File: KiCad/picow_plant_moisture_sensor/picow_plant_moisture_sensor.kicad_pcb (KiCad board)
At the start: 4 copper layers, 94.6 x 64.1 mm, 64 parts, among them J1 Conn_01x03, J10 Conn_01x03, J11 Conn_01x03, J12 Conn_01x03, J13 Conn_02x03_Odd_Even, J14 Conn_01x03, J15 Conn_01x03, J16 Conn_01x03, J17 Conn_01x03, J2 Conn_01x03, J3 Conn_01x03, J4 Conn_01x03, J5 Conn_01x03, J6 Conn_01x03, J7 Conn_01x03, J8 Conn_01x03, J9 Conn_01x03, SW1 SW_Push, SW2 SW_Push, SW3 SW_Push, SW4 SW_Push, U1 ADS1115IDGS, U2 PicoW, U3 ADS1115IDGS, U4 ADS1115IDGS, U5 ADS1115IDGS, U6 24LC16

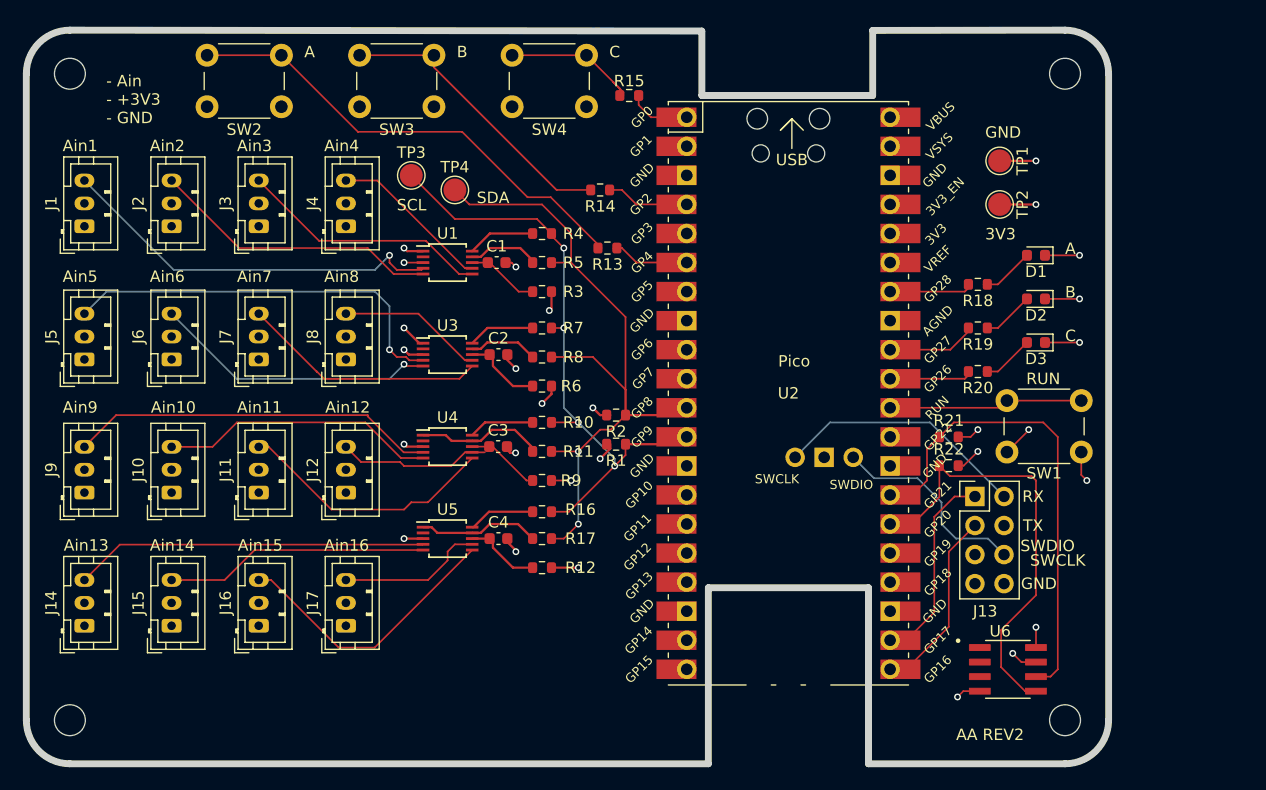
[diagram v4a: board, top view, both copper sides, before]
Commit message: 32 board bring up (#35)
* Add rev2

* Add eeprom cap and I2C test points
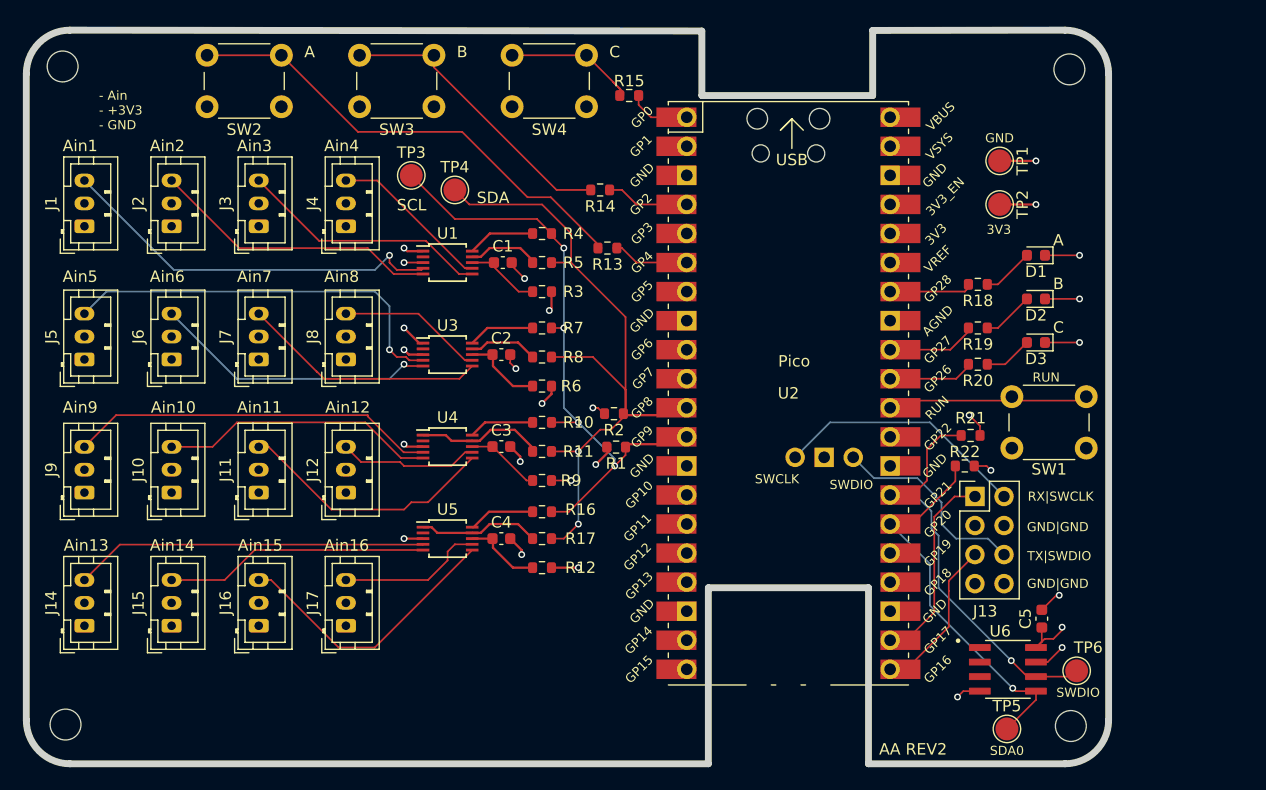
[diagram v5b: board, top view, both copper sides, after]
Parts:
- added C5: 100n, Capacitor_SMD:C_0603_1608Metric, F.Cu at (152.6, 94.7)
- added TP5: TestPoint, TestPoint:TestPoint_Pad_D2.0mm, F.Cu at (149.6, 104.3)
- added TP6: TestPoint, TestPoint:TestPoint_Pad_D2.0mm, F.Cu at (155.7, 99.3)
- moved R21 1.91 mm to (146.4, 78.7)
- moved R22 1.40 mm to (145.9, 81.4)
- moved H2 0.90 mm to (67.0, 46.4)
- moved H3 0.72 mm to (155.2, 104.1)
- moved R20 0.63 mm to (147.1, 72.5)
- moved SW1 0.55 mm to (150.0, 75.3)
- moved H1 0.54 mm to (155.1, 46.7)
- moved H4 0.54 mm to (67.3, 104.0)
- moved C1 0.54 mm to (105.5, 63.6)
- moved C3 0.28 mm to (105.4, 79.7)
- moved C2 0.25 mm to (105.4, 71.6)
- moved C4 0.25 mm to (105.4, 87.7)
- moved R1 0.25 mm to (115.4, 79.7)
- moved R2 0.23 mm to (115.2, 76.8)
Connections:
- J13 pad 3: /GPIO16 -> GND
- J13 pad 5: GND -> /GPIO16
- TP3 pad 1: /SCL -> /GPIO9
- TP4 pad 1: /SDA -> /GPIO8
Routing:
- net /GPIO21: track 41.9 -> 36.6 mm, vias 0 -> 1
- net /GPIO20: track 38.5 -> 33.9 mm, vias 0 -> 1
- net +3V3: track 22.4 -> 25.6 mm
- net GND: track 37.7 -> 34.8 mm, vias 17 -> 16
- net /GPIO16: track 16.5 -> 13.9 mm
- net /AIN8: track 33.3 -> 32.2 mm
- net Net-(D3-A): track 4.83 -> 4.26 mm
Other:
- board text added: "GND|GND"
- board text added: "RX|SWCLK"
- board text added: "SDA0"
- board text added: "TX|SWDIO"
- board text removed: "RX"
- board text removed: "SWCLK"
- board text removed: "TX"

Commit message: Design with RP2040 IC instead of pico board
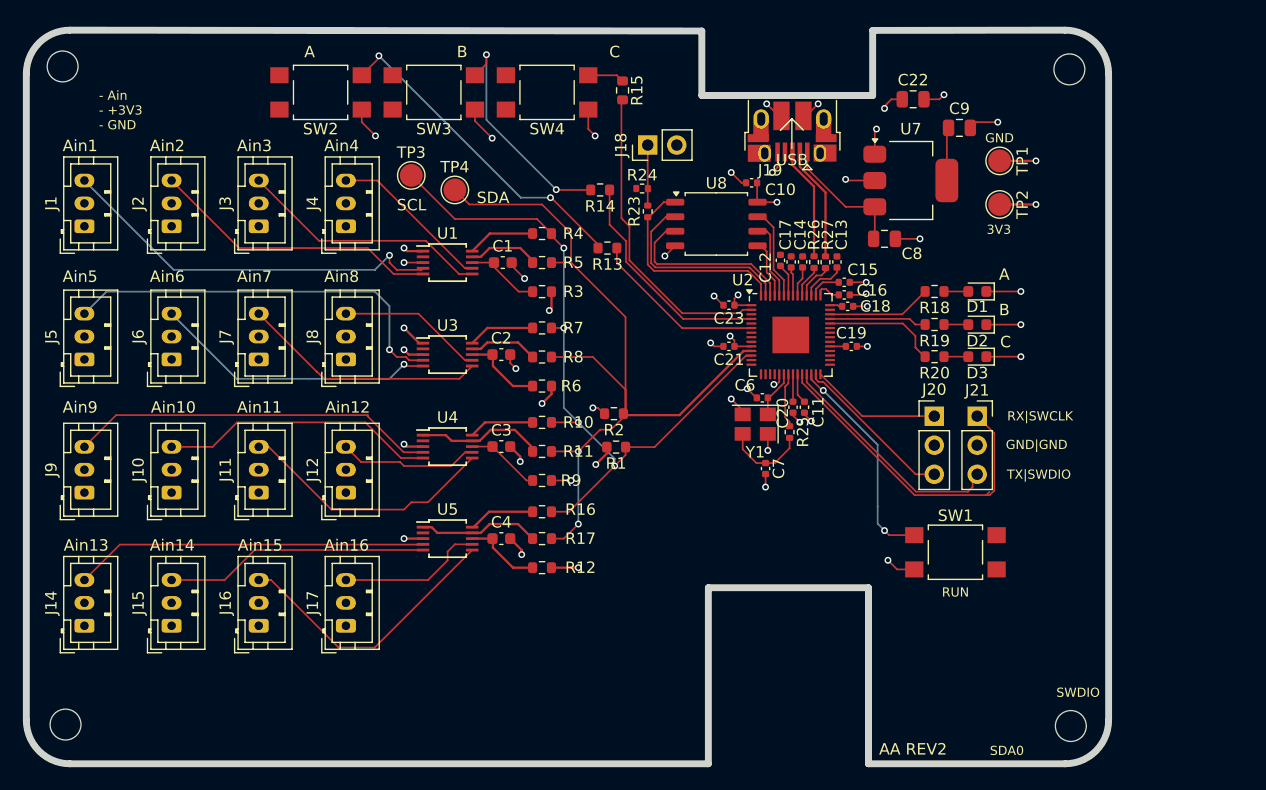
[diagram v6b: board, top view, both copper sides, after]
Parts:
- removed C5: 100n, Capacitor_SMD:C_0603_1608Metric
- removed J13: Conn_02x03_Odd_Even, Connector_PinHeader_2.54mm:PinHeader_2x04_P2.54mm_Vertical
- removed R21, R22: 5k, Resistor_SMD:R_0603_1608Metric
- removed TP5, TP6: TestPoint, TestPoint:TestPoint_Pad_D2.0mm
- removed U6: 24LC16, 24LC16B-I_SN:SOIC127P600X175-8N
- added C10: 100n, Capacitor_SMD:C_0402_1005Metric, F.Cu at (127.3, 56.6)
- added C11: 100n, Capacitor_SMD:C_0402_1005Metric, F.Cu at (131.9, 76.2)
- added C12: 100n, Capacitor_SMD:C_0402_1005Metric, F.Cu at (129.8, 63.4)
- added C13: 1u, Capacitor_SMD:C_0402_1005Metric, F.Cu at (134.7, 63.5)
- added C14: 100n, Capacitor_SMD:C_0402_1005Metric, F.Cu at (131.7, 63.5)
- added C15: 1u, Capacitor_SMD:C_0402_1005Metric, F.Cu at (135.4, 65.3)
- added C16: 100n, Capacitor_SMD:C_0402_1005Metric, F.Cu at (135.4, 66.4)
- added C17: 100n, Capacitor_SMD:C_0402_1005Metric, F.Cu at (130.7, 63.5)
- added C18: 100n, Capacitor_SMD:C_0402_1005Metric, F.Cu at (135.7, 67.4)
- added C19: 100n, Capacitor_SMD:C_0402_1005Metric, F.Cu at (136.0, 70.9)
- added C20: 100n, Capacitor_SMD:C_0402_1005Metric, F.Cu at (130.9, 76.2)
- added C21: 100n, Capacitor_SMD:C_0402_1005Metric, F.Cu at (125.3, 70.9)
- added C22: 10u, Capacitor_SMD:C_0805_2012Metric, F.Cu at (141.4, 49.3)
- added C23: 100n, Capacitor_SMD:C_0402_1005Metric, F.Cu at (125.3, 67.3)
- added C6: 15p, Capacitor_SMD:C_0402_1005Metric, F.Cu at (128.2, 75.4)
- added C7: 15p, Capacitor_SMD:C_0402_1005Metric, F.Cu at (128.5, 81.6)
- added C8: 10u, Capacitor_SMD:C_0805_2012Metric, F.Cu at (138.9, 61.5)
- added C9: 10u, Capacitor_SMD:C_0805_2012Metric, F.Cu at (145.4, 51.8)
- added J18: Conn_01x02, Connector_PinHeader_2.54mm:PinHeader_1x02_P2.54mm_Vertical, F.Cu at (118.2, 53.3)
- added J19: USB_B_Micro, Connector_USB:USB_Micro-B_Amphenol_10103594-0001LF_Horizontal, F.Cu at (130.8, 52.1)
- added J20: Conn_01x03, Connector_PinHeader_2.54mm:PinHeader_1x03_P2.54mm_Vertical, F.Cu at (143.2, 77.0)
- added J21: Conn_01x03, Connector_PinSocket_2.54mm:PinSocket_1x03_P2.54mm_Vertical, F.Cu at (147.0, 77.0)
- added R23: 1k, Resistor_SMD:R_0402_1005Metric, F.Cu at (118.2, 59.1)
- added R24: DNF, Resistor_SMD:R_0402_1005Metric, F.Cu at (117.7, 57.1)
- added R25: 1k, Resistor_SMD:R_0402_1005Metric, F.Cu at (130.6, 78.4)
- added R26: 27, Resistor_SMD:R_0402_1005Metric, F.Cu at (132.7, 63.5)
- added R27: 27, Resistor_SMD:R_0402_1005Metric, F.Cu at (133.7, 63.5)
- added U7: NCP1117-3.3_SOT223, Package_TO_SOT_SMD:SOT-223-3_TabPin2, F.Cu at (141.2, 56.4)
- added U8: W25Q128JVS, Package_SO:SOIC-8_5.23x5.23mm_P1.27mm, F.Cu at (124.2, 60.2)
- added Y1: ABM8-272-T3, Crystal:Crystal_SMD_3225-4Pin_3.2x2.5mm, F.Cu at (127.6, 77.7)
- SW1, SW2, SW3, SW4: footprint Button_Switch_THT:SW_PUSH_6mm -> Button_Switch_SMD:SW_SPST_TL3305A
- U2: value PicoW -> RP2040; footprint RaspberryPI PicoW:RPi_PicoW_SMD_TH -> Package_DFN_QFN:QFN-56-1EP_7x7mm_P0.4mm_EP3.2x3.2mm
- moved SW1 14.5 mm to (145.1, 88.9)
- moved D1 6.02 mm to (147.0, 66.1)
- moved D2 5.60 mm to (147.0, 69.0)
- moved D3 5.28 mm to (147.0, 71.8)
- moved U2 5.10 mm to (130.7, 69.9)
- moved R20 3.84 mm to (143.3, 71.8)
- moved R18 3.84 mm to (143.3, 66.1)
- moved R19 3.80 mm to (143.3, 69.0)
- moved SW4 3.66 mm to (109.4, 48.7)
- moved SW2 3.65 mm to (89.6, 48.7)
- moved SW3 1.25 mm to (99.5, 48.7)
- moved R15 0.73 mm to (116.0, 48.5), turned to 90 degrees
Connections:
- net /GPIO8 renamed /SDA1
- net /GPIO9 renamed /SCL1
- R18 pad 2: /GPIO28 -> /MCU/GPIO28
- R19 pad 2: /GPIO27 -> /MCU/GPIO27
- R20 pad 2: /GPIO26 -> /MCU/GPIO26
- SW1 pad 1: /RUN -> Net-(U2-RUN)
- U2 pad 1: /GPIO0 -> +3V3
- U2 pad 10: /GPIO7 -> +3V3
- U2 pad 13: GND -> unconnected-(U2-GPIO10-Pad13)
- U2 pad 14: /GPIO10 -> unconnected-(U2-GPIO11-Pad14)
- U2 pad 15: /GPIO11 -> unconnected-(U2-GPIO12-Pad15)
- U2 pad 16: /GPIO12 -> unconnected-(U2-GPIO13-Pad16)
- U2 pad 17: /GPIO13 -> unconnected-(U2-GPIO14-Pad17)
- U2 pad 18: GND -> unconnected-(U2-GPIO15-Pad18)
- U2 pad 19: /GPIO14 -> GND
- U2 pad 2: /GPIO1 -> /GPIO0
- U2 pad 20: /GPIO15 -> /MCU/XIN
- U2 pad 21: /GPIO16 -> /MCU/XOUT
- U2 pad 22: /GPIO17 -> +3V3
- U2 pad 23: GND -> +1V1
- U2 pad 24: /GPIO18 -> /MCU/SWCLK
- U2 pad 25: /GPIO19 -> /MCU/SWD
- U2 pad 26: /GPIO20 -> Net-(U2-RUN)
- U2 pad 27: /GPIO21 -> /MCU/UART0_TX
- U2 pad 28: GND -> /MCU/UART0_RX
- U2 pad 29: /GPIO22 -> unconnected-(U2-GPIO18-Pad29)
- U2 pad 3: GND -> unconnected-(U2-GPIO1-Pad3)
- U2 pad 30: /RUN -> unconnected-(U2-GPIO19-Pad30)
- U2 pad 31: /GPIO26 -> unconnected-(U2-GPIO20-Pad31)
- U2 pad 32: /GPIO27 -> unconnected-(U2-GPIO21-Pad32)
- U2 pad 33: GND -> +3V3
- U2 pad 34: /GPIO28 -> unconnected-(U2-GPIO22-Pad34)
- U2 pad 36: +3V3 -> unconnected-(U2-GPIO24-Pad36)
- U2 pad 38: GND -> /MCU/GPIO26
- U2 pad 39: /VSYS -> /MCU/GPIO27
- U2 pad 40: VBUS -> /MCU/GPIO28
- U2 pad 41: /SWCLK -> unconnected-(U2-GPIO29_ADC3-Pad41)
- U2 pad 42: GND -> +3V3
- U2 pad 43: /SWDIO -> +3V3
- U2 pad 5: /GPIO3 -> unconnected-(U2-GPIO3-Pad5)
- U2 pad 7: /GPIO5 -> unconnected-(U2-GPIO5-Pad7)
- U2 pad 8: GND -> unconnected-(U2-GPIO6-Pad8)
- U2 pad 9: /GPIO6 -> unconnected-(U2-GPIO7-Pad9)
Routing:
- net /GPIO21: track 36.6 -> 0.00 mm, vias 1 -> 0
- net /GPIO20: track 33.9 -> 0.00 mm, vias 1 -> 0
- net +3V3: track 25.6 -> 58.1 mm, vias 11 -> 16
- net GND: track 34.8 -> 64.1 mm, vias 16 -> 36
- net /MCU/SWCLK: track 0.00 -> 29.3 mm
- net /SWCLK: track 22.2 -> 0.00 mm
- net /GPIO0: track 5.48 -> 27.1 mm
- net /MCU/SWD: track 0.00 -> 20.6 mm
- net Net-(U2-RUN): track 0.00 -> 19.1 mm, vias 0 -> 2
- net /MCU/QSPI_SS: track 0.00 -> 18.7 mm
- net /SWDIO: track 17.8 -> 0.00 mm
- net /GPIO17: track 17.5 -> 0.00 mm
- net /MCU/QSPI_SD1: track 0.00 -> 17.2 mm
- net /RUN: track 17.0 -> 0.00 mm
- net /MCU/QSPI_SD2: track 0.00 -> 16.3 mm
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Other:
- board text removed: "Pico"
